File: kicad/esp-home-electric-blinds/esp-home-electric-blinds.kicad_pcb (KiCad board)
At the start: 2 copper layers, 66.1 x 91 mm, 14 parts, among them J1 AC_IN, J2 Stepper_2_conn, J3 Stepper_2_conn, J4 Conn_01x05, U1 ESP32_mini, U2 TMC2208_Stepper_driver, U3 TMC2208_Stepper_driver

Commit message: pcb V2
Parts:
- added J5: Stepper_2_conn, connectors_johnymalina:JST_smd_1x04_horizontal, F.Cu at (193.1, 86.7)
- added J6: Stepper_1_conn, connectors_johnymalina:JST_smd_1x04_horizontal, F.Cu at (193.1, 135.7)
- J2, J4: moved to F.Cu
- J3: value Stepper_2_conn -> Stepper_1_conn; moved to F.Cu
- moved H4 144.5 mm to (198.0, 76.0)
- moved J3 140.4 mm to (193.1, 119.3)
- moved U2 116.9 mm to (175.7, 128.0), turned to 180 degrees
- moved H2 104.0 mm to (141.0, 147.0)
- moved J4 89.8 mm to (155.4, 80.8)
- moved J2 86.7 mm to (193.1, 103.0), turned to 90 degrees
- moved U3 82.3 mm to (175.7, 95.7)
- moved PS1 81.0 mm to (150.5, 98.0), turned to 90 degrees
- moved U1 73.6 mm to (151.1, 123.6), turned to 180 degrees
- moved H3 73.5 mm to (198.0, 148.0)
- moved H1 49.4 mm to (102.0, 76.0)
- moved F1 46.3 mm to (132.8, 78.0), turned to 90 degrees
- moved PS2 18.3 mm to (117.5, 112.0)
- moved J1 17.9 mm to (114.7, 146.0)
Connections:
- J4 pad 2: IO_32 -> IO_19
- J4 pad 4: IO_19 -> +3.3V
- U1 pad 28: IO_32 -> EN_PIN_2
- U2 pad JP2_3: Net-(J3-Pin_2) -> Net-(J3-Pin_4)
- U2 pad JP2_4: Net-(J3-Pin_1) -> Net-(J3-Pin_3)
- U2 pad JP2_5: Net-(J3-Pin_3) -> Net-(J3-Pin_2)
- U2 pad JP2_6: Net-(J3-Pin_4) -> Net-(J3-Pin_1)
- U3 pad JP1_8: EN_PIN -> EN_PIN_2
- U3 pad JP2_3: Net-(J2-Pin_2) -> Net-(J2-Pin_4)
- U3 pad JP2_4: Net-(J2-Pin_1) -> Net-(J2-Pin_3)
- U3 pad JP2_5: Net-(J2-Pin_3) -> Net-(J2-Pin_2)
- U3 pad JP2_6: Net-(J2-Pin_4) -> Net-(J2-Pin_1)
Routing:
- net +12V: track 41.7 -> 104.4 mm, vias 0 -> 2
- net EN_PIN_2: track 0.00 -> 62.6 mm, vias 0 -> 2
- net Net-(J3-Pin_1): track 6.93 -> 43.3 mm
- net IO_19: track 15.7 -> 48.8 mm, vias 0 -> 4
- net IO_23: track 24.4 -> 56.5 mm, vias 0 -> 2
- net Net-(J3-Pin_3): track 5.88 -> 37.8 mm
- net DIR_PIN_2: track 71.2 -> 39.6 mm, vias 0 -> 2
- net Net-(J2-Pin_3): track 6.21 -> 36.8 mm
- net STEP_PIN_2: track 69.7 -> 43.0 mm, vias 0 -> 2
- net Net-(J2-Pin_1): track 6.90 -> 33.3 mm
- net DIR_PIN: track 70.4 -> 45.5 mm, vias 0 -> 2
- net STEP_PIN: track 64.5 -> 40.9 mm, vias 1 -> 2
- net Net-(J3-Pin_2): track 15.4 -> 38.2 mm
- net Net-(J2-Pin_2): track 14.6 -> 36.8 mm
- net IO_33: track 29.3 -> 51.1 mm, vias 0 -> 2
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- added copper zone on B.Cu, net AC_L
- added copper zone on B.Cu, net AC_N
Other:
- board size 66.1 x 91 mm -> 100 x 76 mm
- board text removed: "ESPHome Electric Blinds Author:Jakub Cihanek 26.03.2024 V2.0"

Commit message: silkscreen description
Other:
- board text added: "DRV1"
- board text added: "DRV1_OUT"
- board text added: "DRV2"
- board text added: "DRV2_OUT"
- board text added: "ESPHome Smart Blinds V2.0 Author: Jakub Cihanek 24/06/2024"
- board text added: "IO_EXPANSION"

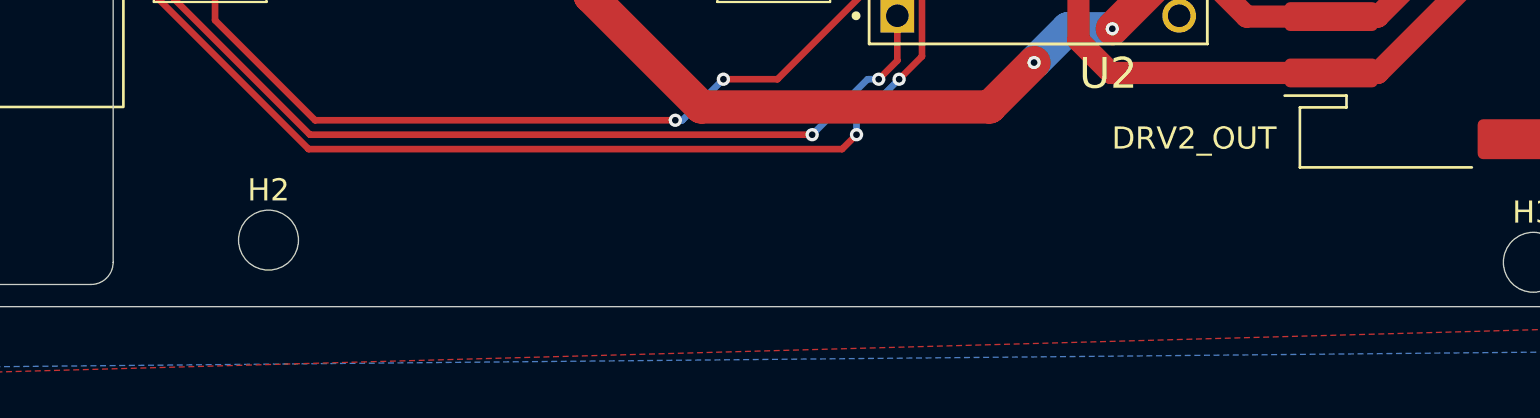
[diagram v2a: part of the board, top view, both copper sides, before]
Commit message: added high voltage warning
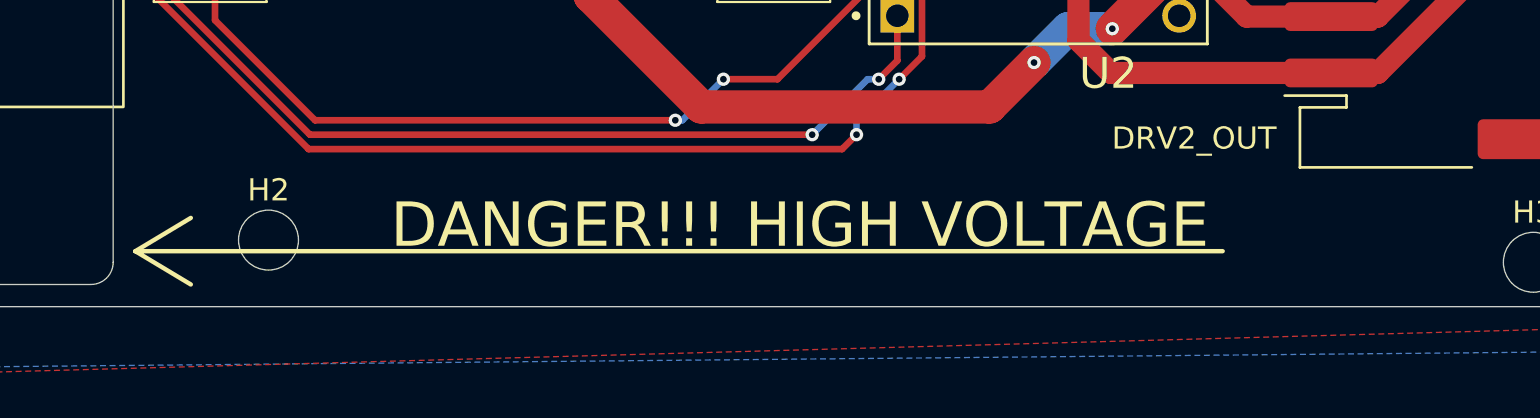
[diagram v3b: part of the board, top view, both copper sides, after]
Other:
- board text added: "DANGER!!! HIGH VOLTAGE"
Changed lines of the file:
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@@
+	)
+	(gr_line
+		(start 135 147.5)
+		(end 137.5 149)
+		(stroke
+			(width 0.2)
+			(type default)
+		)
+		(layer "F.SilkS")
+	)
+	(gr_line
+		(start 135 147.5)
+		(end 184 147.5)
+		(stroke
+			(width 0.2)
+			(type default)
+		)
+		(layer "F.SilkS")
+	)
+	(gr_line
+		(start 137.5 146)
+		(end 135 147.5)
+		(stroke
+			(width 0.2)
+			(type default)
+		)
+		(layer "F.SilkS")
 	)
 	(gr_line
@@
 			(font
 				(size 2.5 2.5)
-				(thickness 0.5)
-				(bold yes)
+				(thickness 0.1)
 			)
 			(justify mirror)
@@
 			)
 			(justify left bottom)
+		)
+	)
+	(gr_text "DANGER!!! HIGH VOLTAGE"
+		(at 146.5 147.5 0)
+		(layer "F.SilkS")
+		(effects
+			(font
+				(size 2 2)
+				(thickness 0.3)
+			)
+			(justify left bottom)
